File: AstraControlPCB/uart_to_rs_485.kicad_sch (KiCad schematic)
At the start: 19 parts, among them U5 SN65HVD1782DR

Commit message: update
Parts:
- removed C17: 47u, LiveAstra:C_0805_2012Metric_Pad1.18x1.45mm_HandSolder, symbol LiveAstra:C_47u_X5R_0805
- added C17: DNP, LiveAstra:C_0805_2012Metric_Pad1.18x1.45mm_HandSolder, symbol LiveAstra:C_DNP_0805
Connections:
- net +3V3: now also C17.2
- net GND: now also C17.1
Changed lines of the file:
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@@
+	)
+	(symbol
+		(lib_id "LiveAstra:C_DNP_0805")
+		(at 63.5 58.42 90)
+		(unit 1)
+		(exclude_from_sim no)
+		(in_bom no)
+		(on_board yes)
+		(dnp yes)
+		(fields_autoplaced yes)
+		(property "Reference" "C17"
+			(at 67.31 55.8799 90)
+			(effects
+				(font
+					(size 1.27 1.27)
+				)
+				(justify right)
+			)
+		)
+		(property "Value" "DNP"
+			(at 67.31 58.42 90)
+			(effects
+				(font
+					(size 1.27 1.27)
+					(bold yes)
+				)
+				(justify right)
+			)
+		)
+		(property "Footprint" "LiveAstra:C_0805_2012Metric_Pad1.18x1.45mm_HandSolder"
+			(at 72.39 58.42 0)
+			(effects
+				(font
+					(size 1.27 1.27)
+				)
+				(hide yes)
+			)
+		)
+		(property "Datasheet" ""
+			(at 76.2 58.42 0)
+			(effects
+				(font
+					(size 1.27 1.27)
+				)
+				(hide yes)
+			)
+		)
+		(property "Description" "Multilayer Ceramic Capacitor"
+			(at 68.58 58.42 0)
+			(effects
+				(font
+					(size 1.27 1.27)
+				)
+				(hide yes)
+			)
+		)
+		(property "LCSC Part" ""
+			(at 80.01 58.42 0)
+			(effects
+				(font
+					(size 1.27 1.27)
+				)
+				(hide yes)
+			)
+		)
+		(property "Extra Values" "0805"
+			(at 67.31 60.9599 90)
+			(effects
+				(font
+					(size 0.762 0.762)
+					(bold yes)
+				)
+				(justify right)
+			)
+		)
+		(pin "1"
+		)
+		(pin "2"
+		)
+		(instances
+			(project ""
+				(path "/9a751838-dce8-4d69-8a02-736625ac74e7/0db21d8e-3390-4d67-877f-0e5d98e37848/670298c9-1a92-4257-b888-4f98b6d49dab"
+					(reference "C17")
+					(unit 1)
+				)
+			)
+		)
 	)
 	(symbol
@@
 					(unit 1)
 				)
-			)
-		)
-	)
-	(symbol
-		(lib_id "LiveAstra:C_47u_X5R_0805")
-		(at 63.5 58.42 90)
-		(unit 1)
-		(exclude_from_sim no)
-		(in_bom no)
-		(on_board yes)
-		(dnp yes)
-		(fields_autoplaced yes)
-		(property "Reference" "C17"
-			(at 67.31 55.8799 90)
-			(effects
-				(font
-					(size 1.27 1.27)
-				)
-				(justify right)
-			)
-		)
-		(property "Value" "47u"
-			(at 67.31 58.42 90)
-			(effects
-				(font
-					(size 1.27 1.27)
-					(bold yes)
-				)
-				(justify right)
-			)
-		)
-		(property "Footprint" "LiveAstra:C_0805_2012Metric_Pad1.18x1.45mm_HandSolder"
-			(at 72.39 58.42 0)
-			(effects
-				(font
-					(size 1.27 1.27)
-				)
-				(hide yes)
-			)
-		)
-		(property "Datasheet" "https://lcsc.com/product-detail/Multilayer-Ceramic-Capacitors-MLCC-SMD-SMT_SAMSUNG_CL21A476MQYNNNE_47uF-476-20-6-3V_C16780.html"
-			(at 76.2 58.42 0)
-			(effects
-				(font
-					(size 1.27 1.27)
-				)
-				(hide yes)
-			)
-		)
-		(property "Description" "Multilayer Ceramic Capacitor"
-			(at 68.58 58.42 0)
-			(effects
-				(font
-					(size 1.27 1.27)
-				)
-				(hide yes)
-			)
-		)
-		(property "LCSC Part" "C16780"
-			(at 80.01 58.42 0)
-			(effects
-				(font
-					(size 1.27 1.27)
-				)
-				(hide yes)
-			)
-		)
-		(property "Extra Values" "6.3V X5R 20% 0805"
-			(at 67.31 60.9599 90)
-			(effects
-				(font
-					(size 0.762 0.762)
-					(bold yes)
-				)
-				(justify right)
-			)
-		)
-		(pin "1"
-		)
-		(pin "2"
-		)
-		(instances
-			(project "AstraControl"
-				(path "/9a751838-dce8-4d69-8a02-736625ac74e7/0db21d8e-3390-4d67-877f-0e5d98e37848/670298c9-1a92-4257-b888-4f98b6d49dab"
-					(reference "C17")
-					(unit 1)
-				)

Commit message: Updates
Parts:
- added R48, R49: DNP, LiveAstra:R_0805_2012Metric_Pad1.20x1.40mm_HandSolder, symbol LiveAstra:R_DNP_0805
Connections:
- net +3V3: now also R48.2, R49.2
- net RS485_RX: now also R48.1
- net RS485_TX: now also R49.1
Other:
- moved on the sheet: R14, R15, TP15, TP16

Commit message: Fixed rs485 for 5v
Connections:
- net +3V3: no longer C17.2, C18.2, C19.2, U5.8 (VCC)
- new net +5V: C17.2, C18.2, C19.2, U5.8 (VCC)
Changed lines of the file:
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@@
+	)
+	(symbol
+		(lib_id "power:+5V")
+		(at 58.42 48.26 0)
+		(unit 1)
+		(exclude_from_sim no)
+		(in_bom yes)
+		(on_board yes)
+		(dnp no)
+		(fields_autoplaced yes)
+		(property "Reference" "#PWR043"
+			(at 58.42 52.07 0)
+			(effects
+				(font
+					(size 1.27 1.27)
+				)
+				(hide yes)
+			)
+		)
+		(property "Value" "+5V"
+			(at 58.42 43.18 0)
+			(effects
+				(font
+					(size 1.27 1.27)
+				)
+			)
+		)
+		(property "Footprint" ""
+			(at 58.42 48.26 0)
+			(effects
+				(font
+					(size 1.27 1.27)
+				)
+				(hide yes)
+			)
+		)
+		(property "Datasheet" ""
+			(at 58.42 48.26 0)
+			(effects
+				(font
+					(size 1.27 1.27)
+				)
+				(hide yes)
+			)
+		)
+		(property "Description" "Power symbol creates a global label with name \"+5V\""
+			(at 58.42 48.26 0)
+			(effects
+				(font
+					(size 1.27 1.27)
+				)
+				(hide yes)
+			)
+		)
+		(pin "1"
+		)
+		(instances
+			(project "AstraControl"
+				(path "/9a751838-dce8-4d69-8a02-736625ac74e7/0db21d8e-3390-4d67-877f-0e5d98e37848/670298c9-1a92-4257-b888-4f98b6d49dab"
+					(reference "#PWR043")
+					(unit 1)
+				)
+			)
+		)
 	)
 	(symbol
@@
 					(unit 1)
 				)
-			)
-		)
-	)
-	(symbol
-		(lib_id "power:+3V3")
-		(at 58.42 48.26 0)
-		(unit 1)
-		(exclude_from_sim no)
-		(in_bom yes)
-		(on_board yes)
-		(dnp no)
-		(fields_autoplaced yes)
-		(property "Reference" "#PWR043"
-			(at 58.42 52.07 0)
-			(effects
-				(font
-					(size 1.27 1.27)
-				)
-				(hide yes)
-			)
-		)
-		(property "Value" "+3V3"
-			(at 58.42 43.18 0)
-			(effects
-				(font
-					(size 1.27 1.27)
-				)
-			)
-		)
-		(property "Footprint" ""
-			(at 58.42 48.26 0)
-			(effects
-				(font
-					(size 1.27 1.27)
-				)
-				(hide yes)
-			)
-		)
-		(property "Datasheet" ""
-			(at 58.42 48.26 0)
-			(effects
-				(font
-					(size 1.27 1.27)
-				)
-				(hide yes)
-			)
-		)
-		(property "Description" "Power symbol creates a global label with name \"+3V3\""
-			(at 58.42 48.26 0)
-			(effects
-				(font
-					(size 1.27 1.27)
-				)
-				(hide yes)
-			)
-		)
-		(pin "1"
-		)
-		(instances
-			(project "AstraControl"
-				(path "/9a751838-dce8-4d69-8a02-736625ac74e7/0db21d8e-3390-4d67-877f-0e5d98e37848/670298c9-1a92-4257-b888-4f98b6d49dab"
-					(reference "#PWR043")
-					(unit 1)
-				)

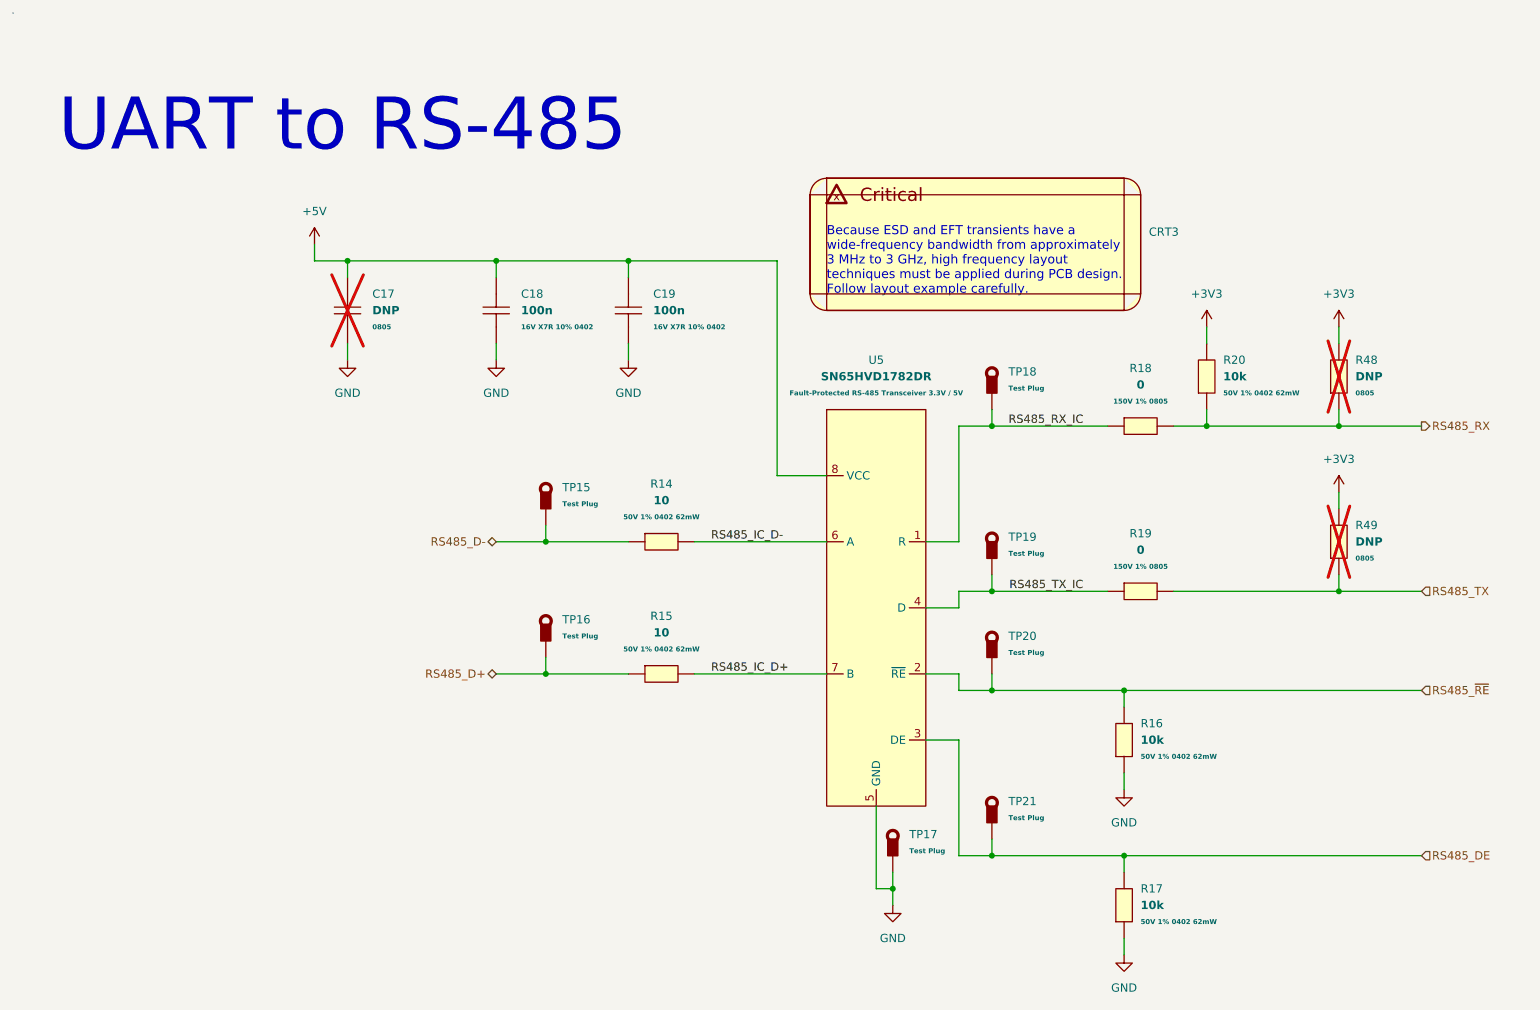
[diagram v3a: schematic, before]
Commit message: RS485 tranceiver changed and TVS
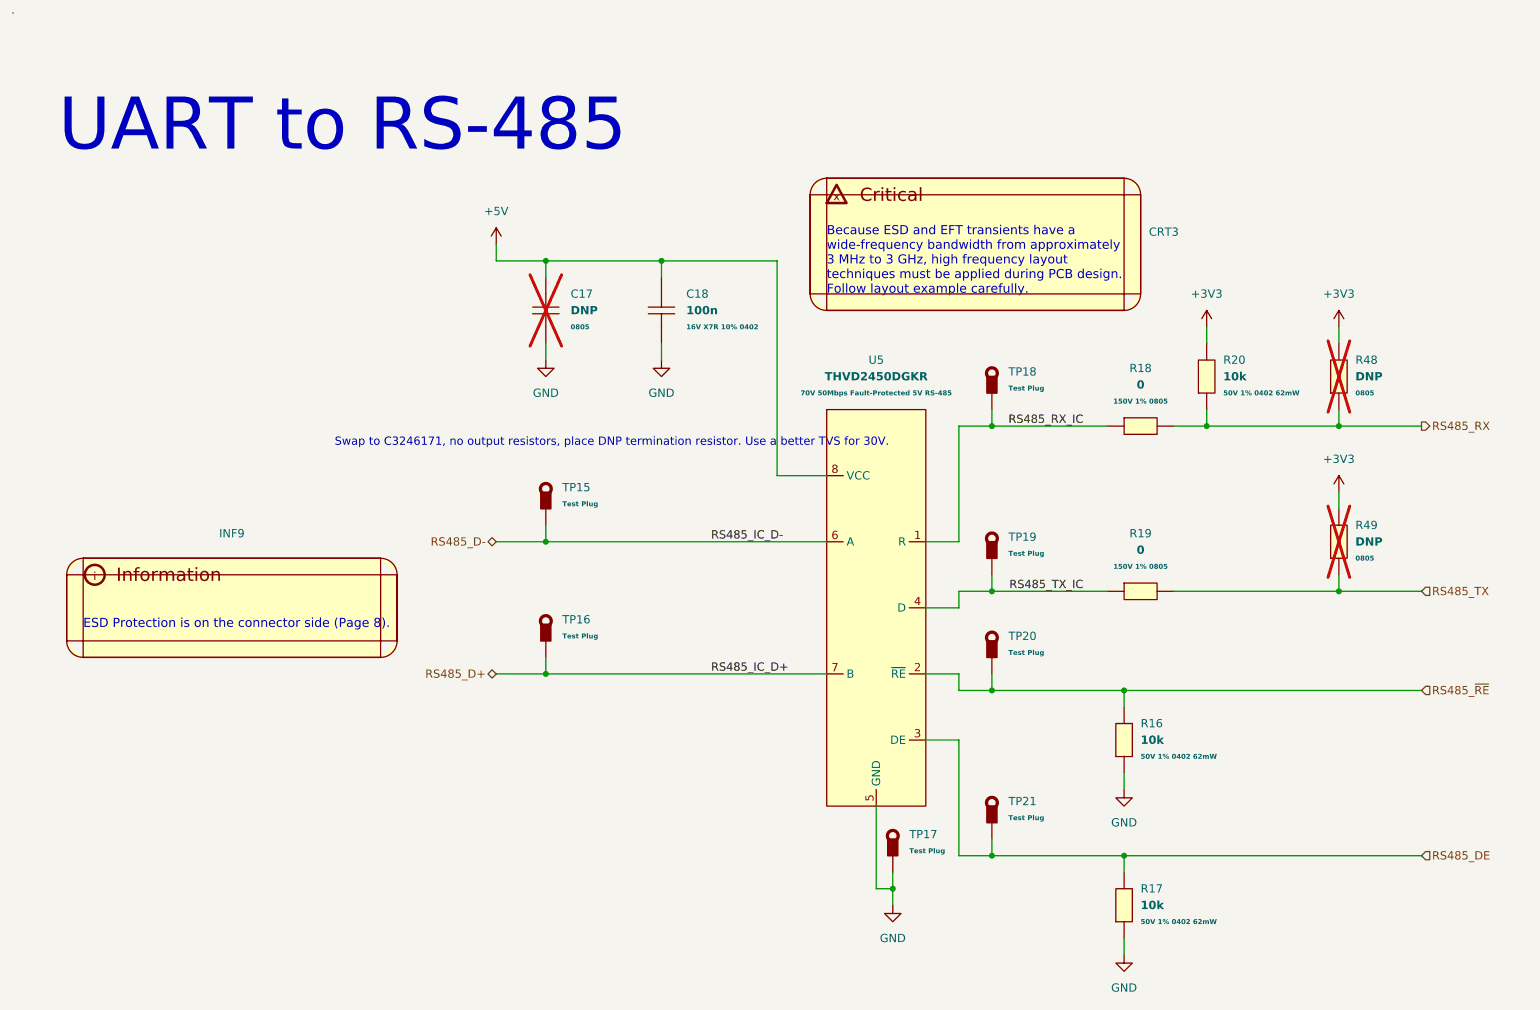
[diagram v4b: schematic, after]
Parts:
- removed C19: 100n, LiveAstra:C_0402_1005Metric, symbol LiveAstra:C_100nF_X7R_0402
- removed R14, R15: 10, LiveAstra:R_0402_1005Metric, symbol LiveAstra:R_10Ohm_0402_62mW
- removed U5: SN65HVD1782DR, LiveAstra:RS_485_SN65HVD1782DR, symbol LiveAstra:U_SN65HVD1782DR_RS485_Transiver_Fault_Protected_SOIC8
- added INF9: ~, symbol LiveAstra:Information_Box
- added U5: THVD2450DGKR, LiveAstra:THVD2450DGKR_RS485_Transciever_VSSOP8, symbol LiveAstra:U_THVD2450DGKR_RS485_Transceiver_MSOP8
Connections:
- net +5V: now also U5.8 (VCC)
- net GND: now also U5.5 (GND)
- net RS485_D+: now also U5.7 (B)
- net RS485_D-: now also U5.6 (A)
- net RS485_DE: now also U5.3 (DE)
- net RS485_RX_IC: now also U5.1 (R)
- net RS485_TX_IC: now also U5.4 (D)
- net RS485_~{RE}: now also U5.2 (~{RE})
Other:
- note added: "ESD Protection is on the connector side (Page 8)."
- note added: "Swap to C3246171, no output resistors, place DNP termination resistor. Use a better TVS for 30V."
- moved on the sheet: C17, C18

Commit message: Reroute complete
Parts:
- removed C17: DNP, LiveAstra:C_0805_2012Metric_Pad1.18x1.45mm_HandSolder, symbol LiveAstra:C_DNP_0805
- added C1: 47u, LiveAstra:C_0805_2012Metric_Pad1.18x1.45mm_HandSolder, symbol LiveAstra:C_47u_X5R_0805
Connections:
- net +5V: now also C1.2
- net GND: now also C1.1
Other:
- note removed: "Swap to C3246171, no output resistors, place DNP termination resistor. Use a better TVS for 30V."
- moved on the sheet: INF9, TP15, TP16

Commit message: Fixed fab layer
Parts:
- R48, R49: footprint LiveAstra:R_0805_2012Metric_Pad1.20x1.40mm_HandSolder -> LiveAstra:R_DNP_0805_2012Metric_Pad1.20x1.40mm_HandSolder
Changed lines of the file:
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@@
 			)
 		)
-		(property "Footprint" "LiveAstra:R_0805_2012Metric_Pad1.20x1.40mm_HandSolder"
+		(property "Footprint" "LiveAstra:R_DNP_0805_2012Metric_Pad1.20x1.40mm_HandSolder"
 			(at 223.52 68.58 0)
 			(effects
@@
 			)
 		)
-		(property "Footprint" "LiveAstra:R_0805_2012Metric_Pad1.20x1.40mm_HandSolder"
+		(property "Footprint" "LiveAstra:R_DNP_0805_2012Metric_Pad1.20x1.40mm_HandSolder"
 			(at 223.52 93.98 0)
 			(effects
